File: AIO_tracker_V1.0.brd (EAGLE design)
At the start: 60 x 55 mm, 75 parts, among them J1 EDGE_ICSP, Q1 MOSFET-PCHANNELSMD, U2 USD-SOCKETNEW, X1 SMA-142-0701-881/886, Y1 ABRACON_ABM3_CRYSTAL

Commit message: fixed some details after receiving the printed pcb
- Fixed size of silkscreen
- Added pin 1 points in silkscreen
- Removed A6 and replaced the SDN of RFM22 with a 3way jumper

Still need to be fixed
- Pressure sensor size in pcb
- Buy the correct SMA Jacks (
http://pt.mouser.com/ProductDetail/Johnson-Cinch-Connectivity-Solutions/142-0701-881/?qs=sGAEpiMZZMuLQf%252bEuFsOrowCuZJUT8YljUsshXITPkY%3d)
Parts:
- added ON----OFF: (no value), SparkFun-Passives:SJ_2
- moved C4 0.45 mm to (-6.50, -1.00)
- renumbered CUTOFF to CUT
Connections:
- removed net A6: U$7.15, U1.19
- new net N$24: U1.19
- new net N$26: ON----OFF.2, U$7.15
- net 3.3V: now also ON----OFF.3
- net GND: now also ON----OFF.1
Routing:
- net A6: track 29.7 -> 0.00 mm, vias 2 -> 0
- net N$26: track 0.00 -> 14.4 mm
- net 3.3V: track 217.0 -> 227.4 mm
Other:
- board text added: "."
- board text added: "3V3"
- board text added: "5V"

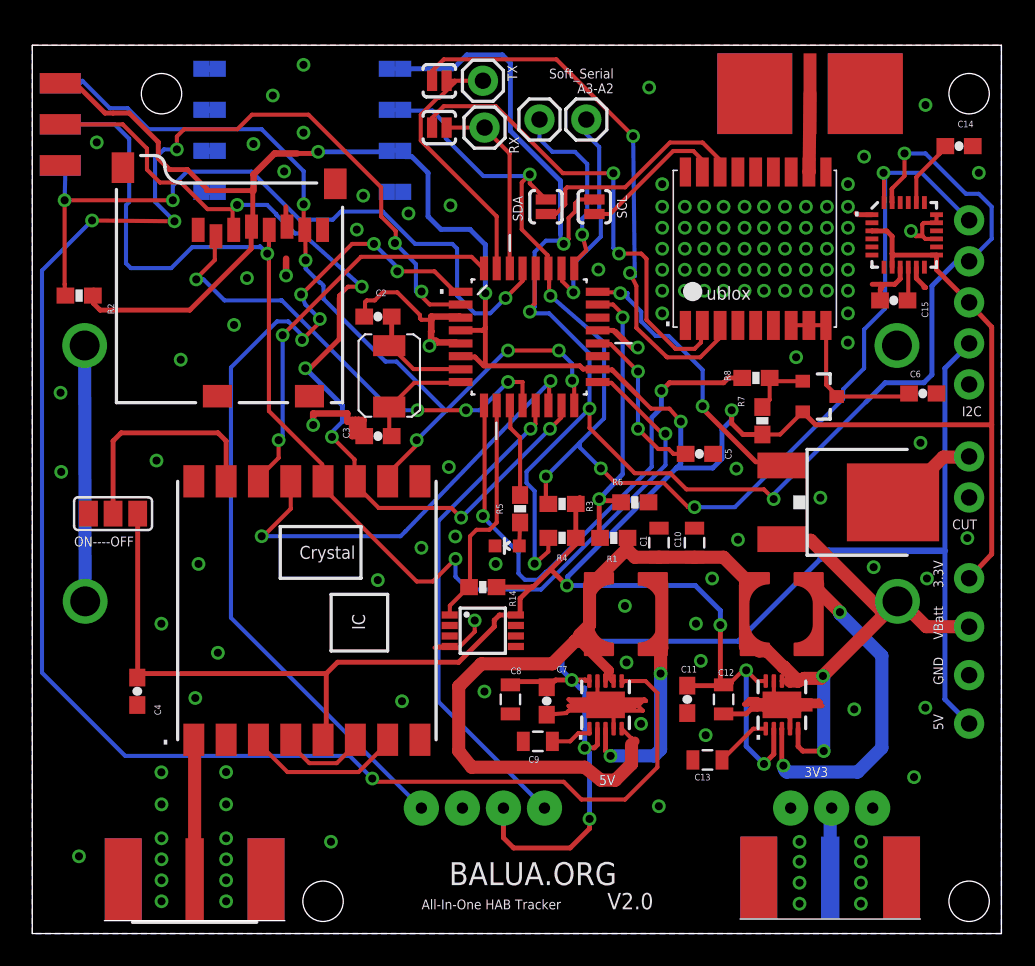
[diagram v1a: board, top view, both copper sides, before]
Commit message: last changes post fabrication
- changed position of the pressure sensor pins (reversed)
- Added more spacing from the AA battery holders
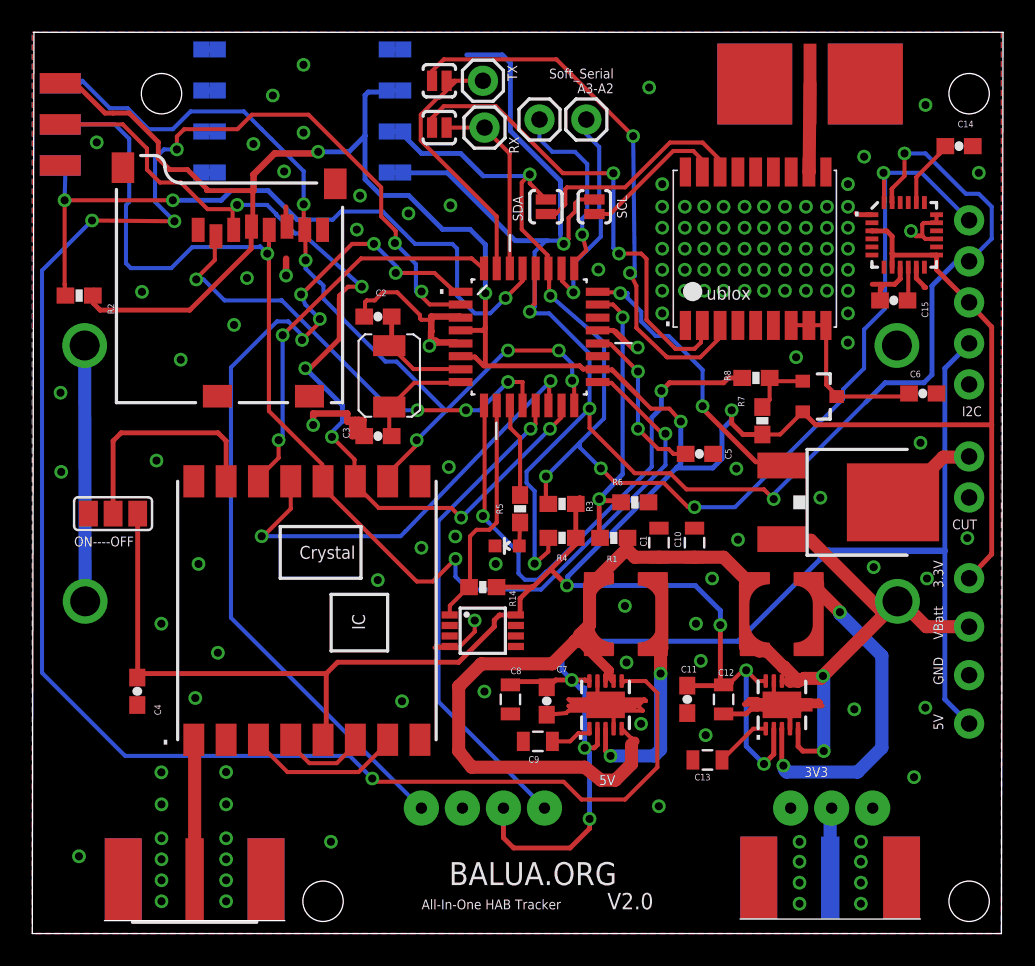
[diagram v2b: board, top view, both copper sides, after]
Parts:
- moved TP10 1.20 mm to (-1.51, 36.2)
- moved TP13 1.20 mm to (-2.53, 38.7)
- moved TP14 1.20 mm to (-1.51, 38.7)
- moved TP5 1.20 mm to (9.96, 36.2)
- moved TP6 1.20 mm to (8.95, 36.2)
- moved TP7 1.20 mm to (9.96, 38.7)
- moved TP8 1.20 mm to (8.95, 38.7)
- moved TP9 1.20 mm to (-2.53, 36.2)
- moved TP1 1.20 mm to (8.95, 31.1)
- moved TP11 1.20 mm to (-1.51, 31.1)
- moved TP12 1.20 mm to (-2.53, 31.1)
- moved TP2 1.20 mm to (9.96, 31.1)
- moved TP15 1.20 mm to (-1.51, 33.7)
- moved TP16 1.20 mm to (-2.53, 33.7)
- moved TP3 1.20 mm to (9.96, 33.7)
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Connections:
- net 3.3V: now also TP5.TP, TP6.TP; no longer TP3.TP, TP4.TP
- net GND: now also TP7.TP, TP8.TP; no longer TP1.TP, TP2.TP
- net SCL: now also TP1.TP, TP2.TP; no longer TP7.TP, TP8.TP
- net SDA: now also TP3.TP, TP4.TP; no longer TP5.TP, TP6.TP
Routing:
- net SCL: track 106.6 -> 113.0 mm
- net 3.3V: track 227.4 -> 232.8 mm
- net GND: track 80.9 -> 82.0 mm, vias 134 -> 135
- net RESET: track 45.2 -> 44.2 mm
- net SDA: track 85.0 -> 84.1 mm
- net MISO: track 54.6 -> 55.5 mm
- net N$3: track 4.85 -> 5.45 mm
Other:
- board size 60 x 55 mm -> 60.1 x 55.8 mm
